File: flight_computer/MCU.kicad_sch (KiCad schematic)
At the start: 22 parts, among them J1 Conn_02x05_Counter_Clockwise, J2 MEM2061-01-188-00-A_REVA, Q1 Q_NPN_BEC, SW1 SW_Push, SW2 SW_Push, U2 STM8S007C8T6, Y1 12MHz

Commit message: ERC complete
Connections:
- no-connect marks 8 -> 22
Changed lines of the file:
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@@
   )
   (no_connect (at 370.84 58.42))
+  (no_connect (at 261.62 156.21))
+  (no_connect (at 261.62 163.83))
+  (no_connect (at 210.82 146.05))
+  (no_connect (at 261.62 158.75))
   (no_connect (at 73.66 182.88))
   (no_connect (at 73.66 190.5))
+  (no_connect (at 210.82 138.43))
   (no_connect (at 73.66 180.34))
+  (no_connect (at 261.62 120.65))
+  (no_connect (at 210.82 143.51))
+  (no_connect (at 210.82 133.35))
+  (no_connect (at 210.82 161.29))
+  (no_connect (at 261.62 138.43))
+  (no_connect (at 261.62 166.37))
+  (no_connect (at 210.82 140.97))
   (no_connect (at 370.84 55.88))
   (no_connect (at 370.84 40.64))
+  (no_connect (at 210.82 125.73))
+  (no_connect (at 210.82 163.83))
   (no_connect (at 33.02 190.5))
   (no_connect (at 370.84 38.1))
@@
     (effects (font (size 1.27 1.27)) (justify left bottom))
   )
-  (label "SCL" (at 181.61 148.59 0)
+  (label "SCL" (at 181.61 148.59 0) (fields_autoplaced)
     (effects (font (size 1.27 1.27)) (justify left bottom))
   )
@@
     (effects (font (size 1.27 1.27)) (justify left bottom))
   )
-  (label "SDA" (at 181.61 151.13 0)
-    (effects (font (size 1.27 1.27)) (justify left bottom))
-  )
+  (label "SDA" (at 181.61 151.13 0) (fields_autoplaced)
+    (effects (font (size 1.27 1.27)) (justify left bottom))
+  )

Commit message: Part way through review
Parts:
- removed J1: Conn_02x05_Counter_Clockwise, symbol Connector_Generic:Conn_02x05_Counter_Clockwise
- added J1: Conn_02x05_Odd_Even, Connector_PinHeader_2.54mm:PinHeader_2x05_P2.54mm_Vertical, symbol Connector_Generic:Conn_02x05_Odd_Even
- U2: value STM8S007C8T6 -> STM8S007C8T6TR; Manufacturer PN (none) -> STM8S007C8T6TR; Supplier (none) -> Digikey; Supplier PN (none) -> 497-18848-1-ND
- renumbered R7 to R8
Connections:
- net 3V3D: now also J1.7 (Pin_7), J1.8 (Pin_8)
- net GND: now also J1.5 (Pin_5), J1.6 (Pin_6)
- net NRST: now also J1.1 (Pin_1)
- net SWIM: now also J1.3 (Pin_3)

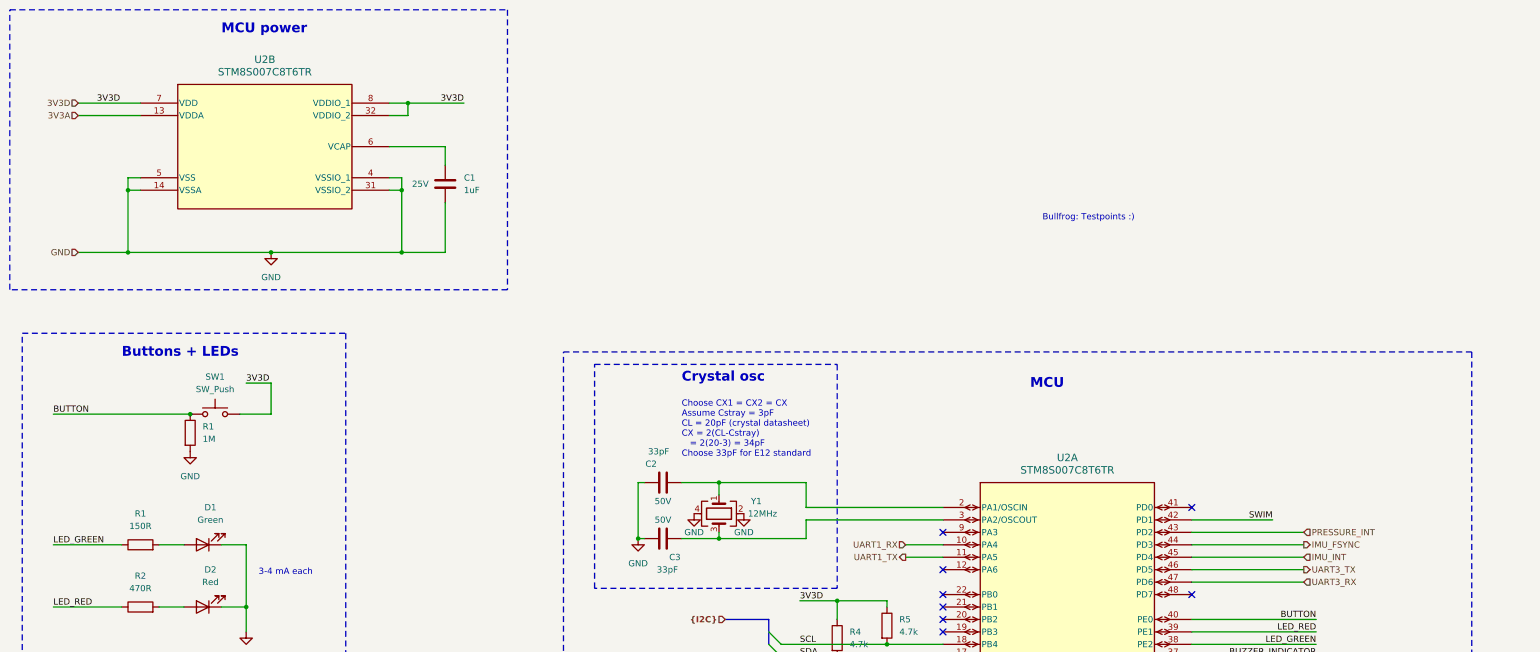
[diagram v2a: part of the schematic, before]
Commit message: Adding shauns thermcoouple
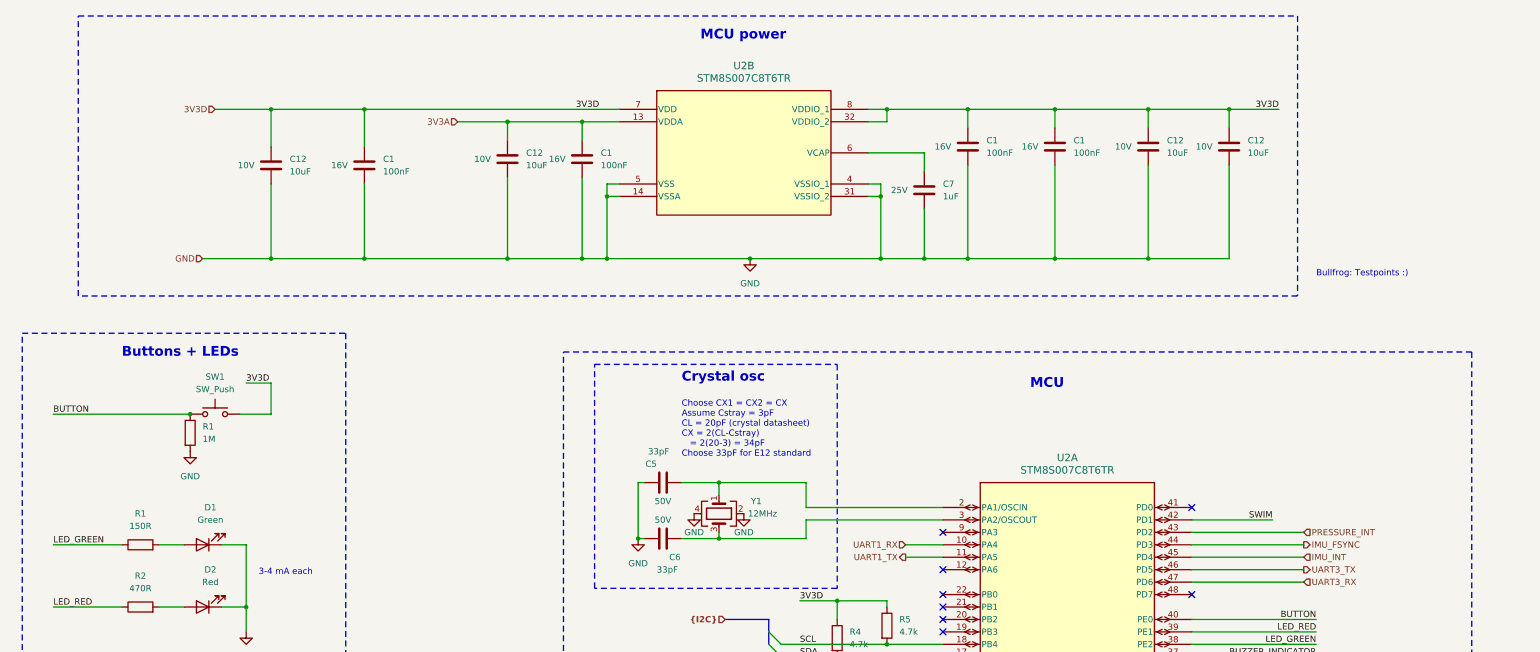
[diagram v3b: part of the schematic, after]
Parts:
- added C1 (x4): 100nF, Capacitor_SMD:C_0402_1005Metric, symbol Device:C
- added C12 (x4): 10uF, Capacitor_SMD:C_0201_0603Metric, symbol Device:C
- renumbered C2 to C5, C3 to C6, C1 to C7
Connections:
- net 3V3A: now also C1.1, C12.1
- net 3V3D: now also C1.1, C1.1, C1.1, C12.1, C12.1, C12.1
- net GND: now also C1.2, C1.2, C1.2, C1.2, C12.2, C12.2, C12.2, C12.2
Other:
- moved on the sheet: C7, U2B

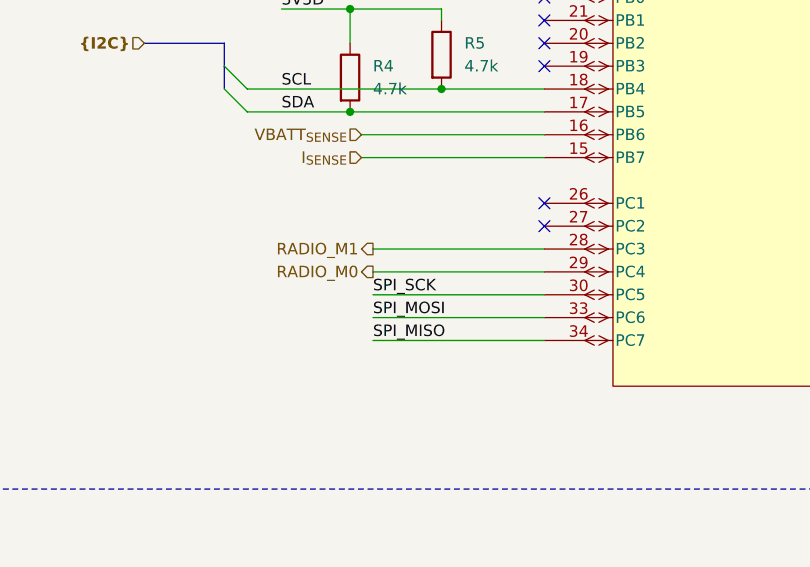
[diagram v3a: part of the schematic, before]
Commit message: Thermocouple circuit done
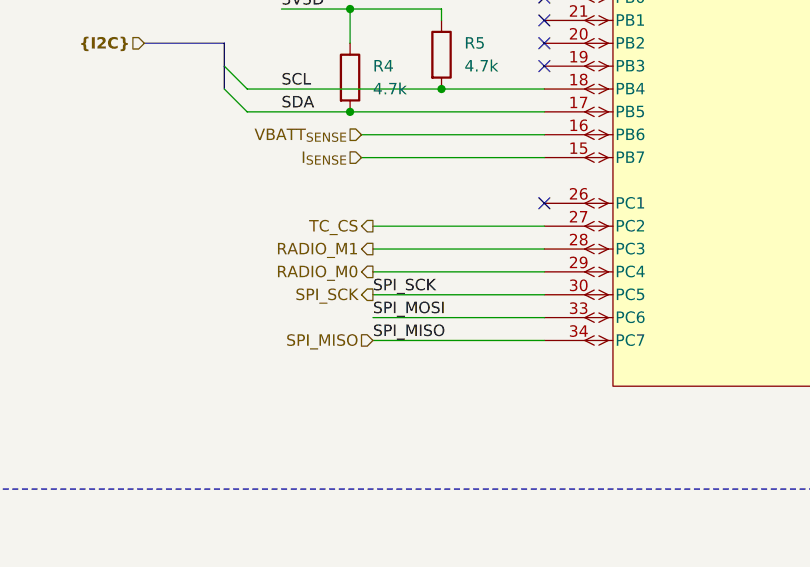
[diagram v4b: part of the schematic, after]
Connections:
- net TC_CS: now reaches U2.27 (PC2)
- no-connect marks 22 -> 21
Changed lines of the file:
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@@
   (no_connect (at 370.84 40.64))
   (no_connect (at 210.82 125.73))
-  (no_connect (at 210.82 163.83))
   (no_connect (at 33.02 190.5))
   (no_connect (at 370.84 38.1))
@@
     (stroke (width 0) (type default))
   )
+  (wire (pts (xy 191.77 163.83) (xy 210.82 163.83))
+    (stroke (width 0) (type default))
+  )
   (wire (pts (xy 233.68 69.85) (xy 252.73 69.85))
     (stroke (width 0) (type default))
@@
     (effects (font (size 1.27 1.27)) (justify left bottom))
   )
+  (hierarchical_label "TC_CS" (shape output) (at 191.77 163.83 180) (fields_autoplaced)
+    (effects (font (size 1.27 1.27)) (justify right))
+  )
   (hierarchical_label "{I2C}" (shape input) (at 166.37 143.51 180) (fields_autoplaced)
     (effects (font (size 1.27 1.27) (thickness 0.254) bold) (justify right))
@@
     (effects (font (size 1.27 1.27)) (justify right))
   )
+  (hierarchical_label "SPI_MISO" (shape input) (at 191.77 176.53 180) (fields_autoplaced)
+    (effects (font (size 1.27 1.27)) (justify right))
+  )
   (hierarchical_label "UART3_TX" (shape output) (at 284.48 133.35 0) (fields_autoplaced)
     (effects (font (size 1.27 1.27)) (justify left))
@@
     (effects (font (size 1.27 1.27)) (justify right))
   )
+  (hierarchical_label "SPI_SCK" (shape output) (at 191.77 171.45 180) (fields_autoplaced)
+    (effects (font (size 1.27 1.27)) (justify right))
+  )

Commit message: Start of layout
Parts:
- C12: footprint Capacitor_SMD:C_0201_0603Metric -> Capacitor_SMD:C_0402_1005Metric
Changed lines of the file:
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@@
       (effects (font (size 1.27 1.27)) (justify left))
     )
-    (property "Footprint" "Capacitor_SMD:C_0201_0603Metric" (at 122.8852 53.34 0)
+    (property "Footprint" "Capacitor_SMD:C_0402_1005Metric" (at 122.8852 53.34 0)
       (effects (font (size 1.27 1.27)) hide)
     )
@@
     )
   )
-  (symbol (lib_id "Device:C") (at 137.16 49.53 0) (unit 1)
-    (in_bom yes) (on_board yes) (dnp no)
-    (property "Reference" "C1" (at 140.97 48.26 0)
-      (effects (font (size 1.27 1.27)) (justify left))
-    )
-    (property "Value" "100nF" (at 140.97 50.8 0)
-      (effects (font (size 1.27 1.27)) (justify left))
-    )
-    (property "Footprint" "Capacitor_SMD:C_0402_1005Metric" (at 138.1252 53.34 0)
+  (symbol (lib_id "Device:C") (at 137.16 49.53 0) (mirror y) (unit 1)
+    (in_bom yes) (on_board yes) (dnp no)
+    (property "Reference" "C1" (at 133.35 48.26 0)
+      (effects (font (size 1.27 1.27)) (justify left))
+    )
+    (property "Value" "100nF" (at 133.35 50.8 0)
+      (effects (font (size 1.27 1.27)) (justify left))
+    )
+    (property "Footprint" "Capacitor_SMD:C_0402_1005Metric" (at 136.1948 53.34 0)
       (effects (font (size 1.27 1.27)) hide)
     )
@@
       (effects (font (size 1.27 1.27)) hide)
     )
-    (property "Voltage" "16V" (at 132.08 49.53 0)
+    (property "Voltage" "16V" (at 142.24 49.53 0)
       (effects (font (size 1.27 1.27)))
     )
@@
       (effects (font (size 1.27 1.27)) (justify left))
     )
-    (property "Footprint" "Capacitor_SMD:C_0201_0603Metric" (at 253.6952 50.8 0)
+    (property "Footprint" "Capacitor_SMD:C_0402_1005Metric" (at 253.6952 50.8 0)
       (effects (font (size 1.27 1.27)) hide)
     )
@@
       (effects (font (size 1.27 1.27)) (justify left))
     )
-    (property "Footprint" "Capacitor_SMD:C_0201_0603Metric" (at 74.6252 54.61 0)
+    (property "Footprint" "Capacitor_SMD:C_0402_1005Metric" (at 74.6252 54.61 0)
       (effects (font (size 1.27 1.27)) hide)
     )
@@
       (effects (font (size 1.27 1.27)) (justify left))
     )
-    (property "Footprint" "Capacitor_SMD:C_0201_0603Metric" (at 270.2052 50.8 0)
-      (effects (font (size 1.27 1.27)) hide)
-    )
+    (property "Footprint" "Capacitor_SMD:C_0402_1005Metric" (at 270.2052 50.8 0)
+      (effects (font (size 1.27 1.27)) hide)
+    )

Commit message: Layout first effort done
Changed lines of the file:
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@@
     )
   )
-  (symbol (lib_id "Device:C") (at 137.16 49.53 0) (mirror y) (unit 1)
+  (symbol (lib_id "Device:C") (at 137.16 49.53 0) (unit 1)
     (in_bom yes) (on_board yes) (dnp no)
-    (property "Reference" "C1" (at 133.35 48.26 0)
+    (property "Reference" "C1" (at 140.97 48.26 0)
       (effects (font (size 1.27 1.27)) (justify left))
     )
-    (property "Value" "100nF" (at 133.35 50.8 0)
+    (property "Value" "100nF" (at 140.97 50.8 0)
       (effects (font (size 1.27 1.27)) (justify left))
     )
-    (property "Footprint" "Capacitor_SMD:C_0402_1005Metric" (at 136.1948 53.34 0)
+    (property "Footprint" "Capacitor_SMD:C_0402_1005Metric" (at 138.1252 53.34 0)
       (effects (font (size 1.27 1.27)) hide)
     )
@@
       (effects (font (size 1.27 1.27)) hide)
     )
-    (property "Voltage" "16V" (at 142.24 49.53 0)
+    (property "Voltage" "16V" (at 132.08 49.53 0)
       (effects (font (size 1.27 1.27)))
     )

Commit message: More PCB layout
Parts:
- added TP1, TP2, TP3, TP4, TP5, TP6, TP7: TestPoint, Connector_PinHeader_2.54mm:PinHeader_1x01_P2.54mm_Vertical, symbol Connector:TestPoint
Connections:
- net SCL: now also TP6.1
- net SDA: now also TP7.1
- net SPI_MISO: now also TP1.1
- net SPI_MOSI: now also TP2.1
- net SPI_NSS: now also TP4.1
- net SPI_SCK: now also TP3.1
- net TC_CS: now also TP5.1

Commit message: Most of the way through relayout and new antenna
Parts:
- added C1: 100nF, Capacitor_SMD:C_0402_1005Metric, symbol Device:C
- added R12 (x5): 10k, Resistor_SMD:R_0402_1005Metric, symbol Device:R
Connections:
- net 3V3D: now also C1.1, R12.2, R12.2, R12.2, R12.2, R12.2
- net GND: now also C1.2
- net SPI_MISO: now also R12.1
- net SPI_MOSI: now also R12.1
- net SPI_NSS: now also R12.1
- net at J2.1 (DAT2): now also R12.1
- net at J2.8 (DAT1): now also R12.1
- no-connect marks 21 -> 19
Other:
- note removed: "Bullfrog: Testpoints :)"
